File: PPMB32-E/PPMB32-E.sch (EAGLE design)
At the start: 36 parts, among them IC1 7805TV, IC2 LM3940IT-3.3, K1 ARK500/2, K2 ARK500/2, K3 ARK500/2, K4 ARK500/2, K5 ARK500/2, U1 ESP32-DEVKITC-32D

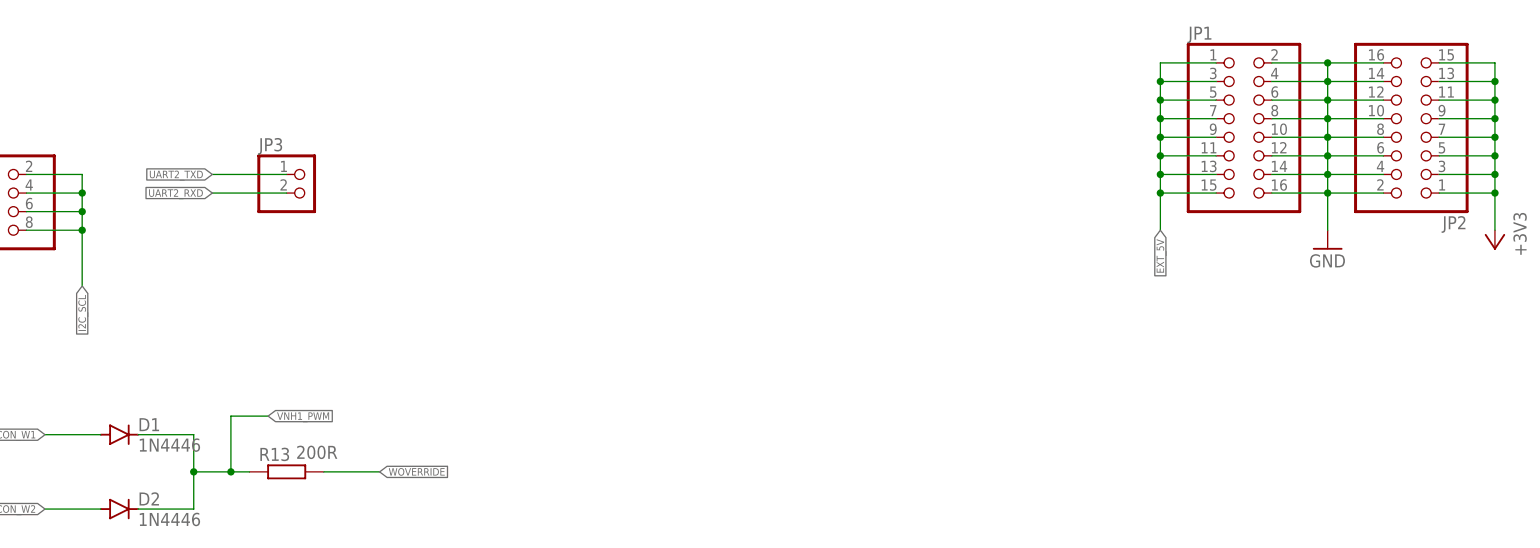
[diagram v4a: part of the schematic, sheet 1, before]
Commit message: Add pins connected to remaining GPIOs on ESP32devkitC
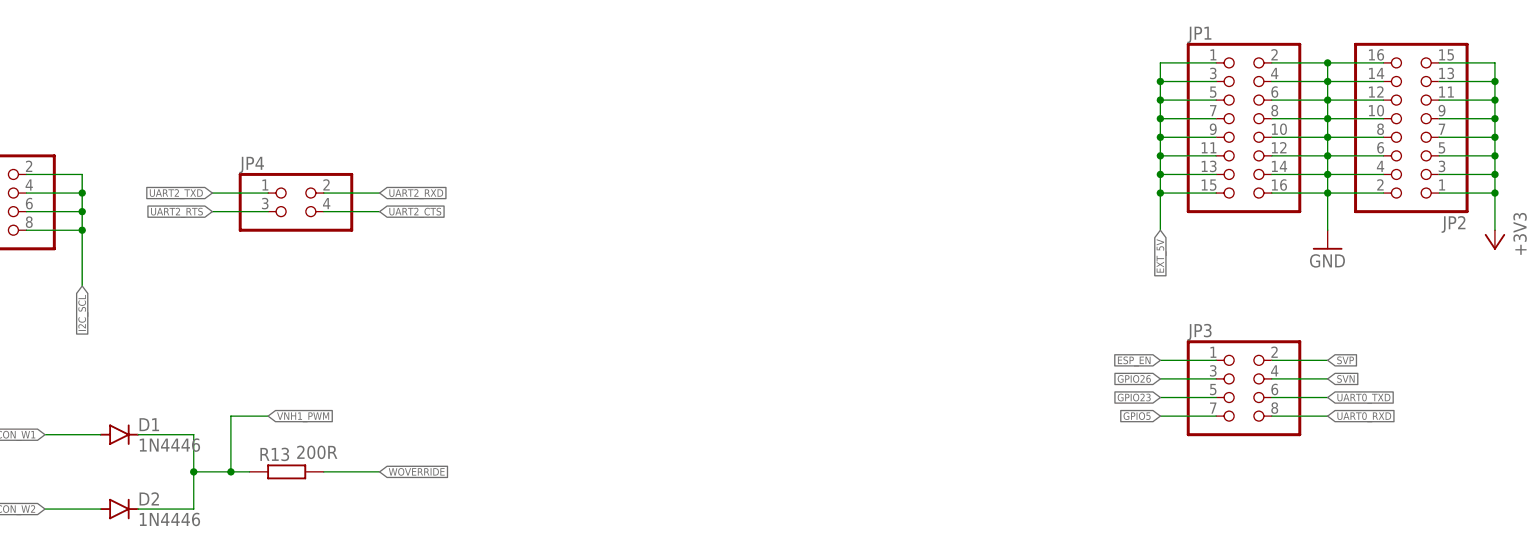
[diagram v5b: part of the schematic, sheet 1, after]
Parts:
- added JP4: (no value), pinhead:PINHD-2X2
- JP3: device pinhead:PINHD-1X2 -> pinhead:PINHD-2X4
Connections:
- net ESP_EN: now also JP3.1
- net GPIO23: now also JP3.5
- net GPIO26: now also JP3.3
- net GPIO5: now also JP3.7
- net SVN: now also JP3.4
- net SVP: now also JP3.2
- net UART0_RXD: now also JP3.8
- net UART0_TXD: now also JP3.6
- net UART2_CTS: now also JP4.4
- net UART2_RTS: now also JP4.3
- net UART2_RXD: now also JP4.2; no longer JP3.2
- net UART2_TXD: now also JP4.1; no longer JP3.1
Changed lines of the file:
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@@
 <setting verticaltext="up"/>
 </settings>
-<grid distance="0.1" unitdist="inch" unit="inch" style="lines" multiple="1" display="no" altdistance="0.01" altunitdist="inch" altunit="inch"/>
+<grid distance="0.1" unitdist="inch" unit="mm" style="lines" multiple="1" display="yes" altdistance="0.01" altunitdist="inch" altunit="mm"/>
 <layers>
 <layer number="1" name="Top" color="4" fill="1" visible="no" active="no"/>
@@
 <part name="R8" library="rcl" library_urn="urn:adsk.eagle:library:334" deviceset="R-EU_" device="R0603" package3d_urn="urn:adsk.eagle:package:23555/3" value="1k"/>
 <part name="GND13" library="supply1" library_urn="urn:adsk.eagle:library:371" deviceset="GND" device=""/>
-<part name="JP3" library="pinhead" library_urn="urn:adsk.eagle:library:325" deviceset="PINHD-1X2" device="" package3d_urn="urn:adsk.eagle:package:22435/2"/>
 <part name="PANCON" library="pinhead" library_urn="urn:adsk.eagle:library:325" deviceset="PINHD-2X6" device="" package3d_urn="urn:adsk.eagle:package:22474/2"/>
 <part name="GND14" library="supply1" library_urn="urn:adsk.eagle:library:371" deviceset="GND" device=""/>
@@
 <part name="GND15" library="supply1" library_urn="urn:adsk.eagle:library:371" deviceset="GND" device=""/>
 <part name="+3V5" library="supply1" library_urn="urn:adsk.eagle:library:371" deviceset="+3V3" device=""/>
+<part name="JP4" library="pinhead" library_urn="urn:adsk.eagle:library:325" deviceset="PINHD-2X2" device="" package3d_urn="urn:adsk.eagle:package:22455/2"/>
+<part name="JP3" library="pinhead" library_urn="urn:adsk.eagle:library:325" deviceset="PINHD-2X4" device="" package3d_urn="urn:adsk.eagle:package:22461/2"/>
 </parts>
 <sheets>
@@
 <attribute name="VALUE" x="312.42" y="160.02" size="1.778" layer="96"/>
 </instance>
-<instance part="JP3" gate="G$1" x="124.46" y="104.14" smashed="yes">
-<attribute name="NAME" x="118.11" y="109.855" size="1.778" layer="95"/>
-<attribute name="VALUE" x="118.11" y="99.06" size="1.778" layer="96"/>
-</instance>
 <instance part="PANCON" gate="A" x="43.18" y="71.12" smashed="yes">
 <attribute name="NAME" x="36.83" y="79.375" size="1.778" layer="95"/>
@@
 <instance part="+3V5" gate="G$1" x="314.96" y="88.9" smashed="yes" rot="R180">
 <attribute name="VALUE" x="312.42" y="88.9" size="1.778" layer="96" rot="R90"/>
+</instance>
+<instance part="JP4" gate="A" x="124.46" y="101.6" smashed="yes">
+<attribute name="NAME" x="115.57" y="107.315" size="1.778" layer="95"/>
+<attribute name="VALUE" x="115.57" y="96.52" size="1.778" layer="96"/>
+</instance>
+<instance part="JP3" gate="A" x="251.46" y="76.2" smashed="yes">
+<attribute name="NAME" x="245.11" y="84.455" size="1.778" layer="95"/>
+<attribute name="VALUE" x="245.11" y="68.58" size="1.778" layer="96"/>
 </instance>
 </instances>
@@
 <label x="83.82" y="195.58" size="1.016" layer="95" rot="R180" xref="yes"/>
 </segment>
+<segment>
+<pinref part="JP3" gate="A" pin="1"/>
+<wire x1="248.92" y1="81.28" x2="241.3" y2="81.28" width="0.1524" layer="91"/>
+<label x="241.3" y="81.28" size="1.016" layer="95" rot="R180" xref="yes"/>
+</segment>
 </net>
 <net name="VNH1_OUTA" class="0">
@@
 <net name="UART2_TXD" class="0">
 <segment>
-<pinref part="JP3" gate="G$1" pin="1"/>
-<wire x1="121.92" y1="106.68" x2="111.76" y2="106.68" width="0.1524" layer="91"/>
-<label x="111.76" y="106.68" size="1.016" layer="95" rot="R180" xref="yes"/>
-</segment>
-<segment>
 <pinref part="U1" gate="G$1" pin="IO16"/>
 <wire x1="132.08" y1="170.18" x2="139.7" y2="170.18" width="0.1524" layer="91"/>
 <label x="139.7" y="170.18" size="1.016" layer="95" xref="yes"/>
 </segment>
+<segment>
+<pinref part="JP4" gate="A" pin="1"/>
+<wire x1="119.38" y1="104.14" x2="111.76" y2="104.14" width="0.1524" layer="91"/>
+<label x="111.76" y="104.14" size="1.016" layer="95" rot="R180" xref="yes"/>
+</segment>
 </net>
 <net name="UART2_RXD" class="0">
-<segment>
-<pinref part="JP3" gate="G$1" pin="2"/>
-<wire x1="121.92" y1="104.14" x2="111.76" y2="104.14" width="0.1524" layer="91"/>
-<label x="111.76" y="104.14" size="1.016" layer="95" rot="R180" xref="yes"/>
-</segment>
 <segment>
 <pinref part="U1" gate="G$1" pin="IO17"/>
 <wire x1="132.08" y1="172.72" x2="139.7" y2="172.72" width="0.1524" layer="91"/>
 <label x="139.7" y="172.72" size="1.016" layer="95" xref="yes"/>
+</segment>
+<segment>
+<pinref part="JP4" gate="A" pin="2"/>
+<wire x1="127" y1="104.14" x2="134.62" y2="104.14" width="0.1524" layer="91"/>
+<label x="134.62" y="104.14" size="1.016" layer="95" xref="yes"/>
 </segment>
 </net>
@@
 <label x="83.82" y="193.04" size="1.016" layer="95" rot="R180" xref="yes"/>
 </segment>
+<segment>
+<pinref part="JP3" gate="A" pin="2"/>
+<wire x1="256.54" y1="81.28" x2="264.16" y2="81.28" width="0.1524" layer="91"/>
+<label x="264.16" y="81.28" size="1.016" layer="95" xref="yes"/>
+</segment>
 </net>
 <net name="SVN" class="0">
@@
 <label x="83.82" y="190.5" size="1.016" layer="95" rot="R180" xref="yes"/>
 </segment>
+<segment>
+<pinref part="JP3" gate="A" pin="4"/>
+<wire x1="256.54" y1="78.74" x2="264.16" y2="78.74" width="0.1524" layer="91"/>
+<label x="264.16" y="78.74" size="1.016" layer="95" xref="yes"/>
+</segment>
 </net>
 <net name="GPIO26" class="0">
@@
 <label x="83.82" y="175.26" size="1.016" layer="95" rot="R180" xref="yes"/>
 </segment>
+<segment>
+<pinref part="JP3" gate="A" pin="3"/>
+<wire x1="248.92" y1="78.74" x2="241.3" y2="78.74" width="0.1524" layer="91"/>
+<label x="241.3" y="78.74" size="1.016" layer="95" rot="R180" xref="yes"/>
+</segment>
 </net>
 <net name="INTERNAL_SENS" class="0">
@@
 <label x="139.7" y="175.26" size="1.016" layer="95" xref="yes"/>
 </segment>
+<segment>
+<pinref part="JP3" gate="A" pin="7"/>
+<wire x1="248.92" y1="73.66" x2="241.3" y2="73.66" width="0.1524" layer="91"/>
+<label x="241.3" y="73.66" size="1.016" layer="95" rot="R180" xref="yes"/>
+</segment>
 </net>
 <net name="UART2_RTS" class="0">
@@
 <label x="139.7" y="177.8" size="1.016" layer="95" xref="yes"/>
 </segment>
+<segment>
+<pinref part="JP4" gate="A" pin="3"/>
+<wire x1="119.38" y1="101.6" x2="111.76" y2="101.6" width="0.1524" layer="91"/>
+<label x="111.76" y="101.6" size="1.016" layer="95" rot="R180" xref="yes"/>
+</segment>
 </net>
 <net name="UART2_CTS" class="0">
@@
 <label x="139.7" y="180.34" size="1.016" layer="95" xref="yes"/>
 </segment>
+<segment>
+<pinref part="JP4" gate="A" pin="4"/>
+<wire x1="127" y1="101.6" x2="134.62" y2="101.6" width="0.1524" layer="91"/>
+<label x="134.62" y="101.6" size="1.016" layer="95" xref="yes"/>
+</segment>
 </net>
 <net name="UART0_RXD" class="0">
@@
 <label x="139.7" y="187.96" size="1.016" layer="95" xref="yes"/>
 </segment>
+<segment>
+<pinref part="JP3" gate="A" pin="8"/>
+<wire x1="256.54" y1="73.66" x2="264.16" y2="73.66" width="0.1524" layer="91"/>
+<label x="264.16" y="73.66" size="1.016" layer="95" xref="yes"/>
+</segment>
 </net>
 <net name="UART0_TXD" class="0">
@@
 <label x="139.7" y="190.5" size="1.016" layer="95" xref="yes"/>
 </segment>
+<segment>
+<pinref part="JP3" gate="A" pin="6"/>
+<wire x1="256.54" y1="76.2" x2="264.16" y2="76.2" width="0.1524" layer="91"/>
+<label x="264.16" y="76.2" size="1.016" layer="95" xref="yes"/>
+</segment>
 </net>
 <net name="GPIO23" class="0">
@@
 <label x="139.7" y="195.58" size="1.016" layer="95" xref="yes"/>
 </segment>
-</net>
+<segment>
+<pinref part="JP3" gate="A" pin="5"/>
+<wire x1="248.92" y1="76.2" x2="241.3" y2="76.2" width="0.1524" layer="91"/>
+<label x="241.3" y="76.2" size="1.016" layer="95" rot="R180" xref="yes"/>
+</segment>
+</net>

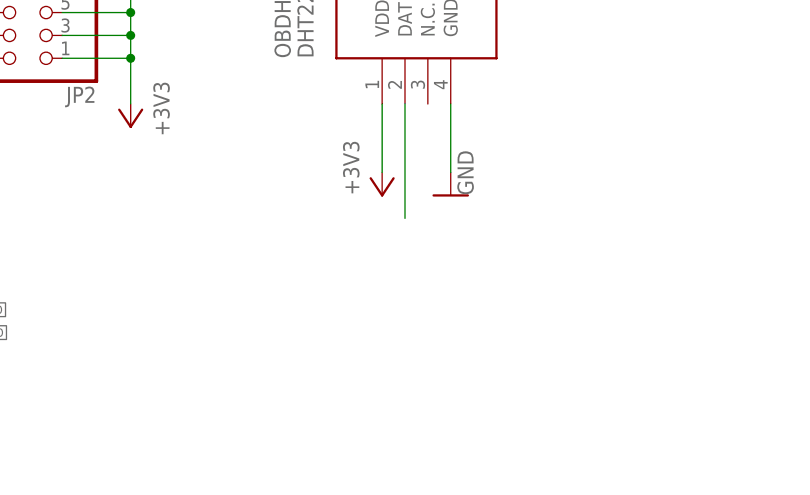
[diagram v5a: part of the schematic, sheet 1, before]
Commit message: Edit silkscreen on PPMB32-E
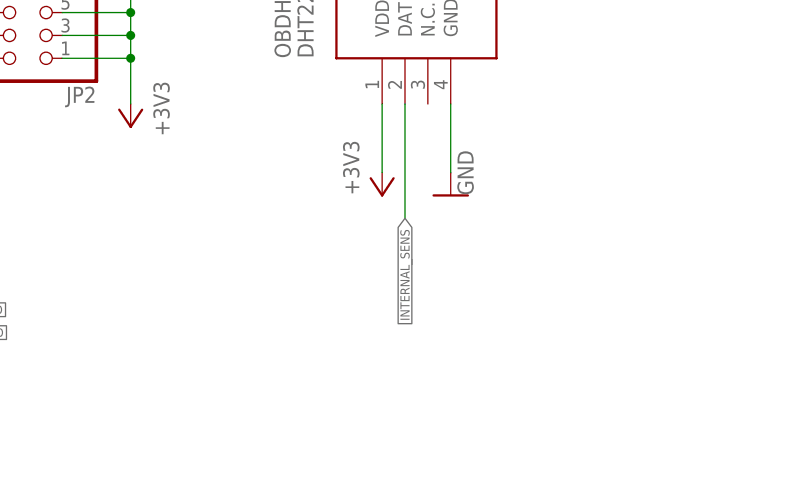
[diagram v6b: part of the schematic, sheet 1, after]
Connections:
- removed net N$13: OBDHT.DAT
- net INTERNAL_SENS: now also OBDHT.DAT
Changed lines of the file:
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@@
 <setting verticaltext="up"/>
 </settings>
-<grid distance="0.1" unitdist="inch" unit="mm" style="lines" multiple="1" display="yes" altdistance="0.01" altunitdist="inch" altunit="mm"/>
+<grid distance="0.1" unitdist="inch" unit="inch" style="lines" multiple="1" display="no" altdistance="0.01" altunitdist="inch" altunit="inch"/>
 <layers>
 <layer number="1" name="Top" color="4" fill="1" visible="no" active="no"/>
@@
 <label x="83.82" y="162.56" size="1.016" layer="95" rot="R180" xref="yes"/>
 </segment>
+<segment>
+<pinref part="OBDHT" gate="G$1" pin="DAT"/>
+<wire x1="317.5" y1="99.06" x2="317.5" y2="86.36" width="0.1524" layer="91"/>
+<label x="317.5" y="86.36" size="1.016" layer="95" rot="R270" xref="yes"/>
+</segment>
 </net>
 <net name="ONE_WIRE" class="0">
@@
 </segment>
 </net>
-<net name="N$13" class="0">
-<segment>
-<pinref part="OBDHT" gate="G$1" pin="DAT"/>
-<wire x1="317.5" y1="99.06" x2="317.5" y2="86.36" width="0.1524" layer="91"/>
-</segment>
-</net>

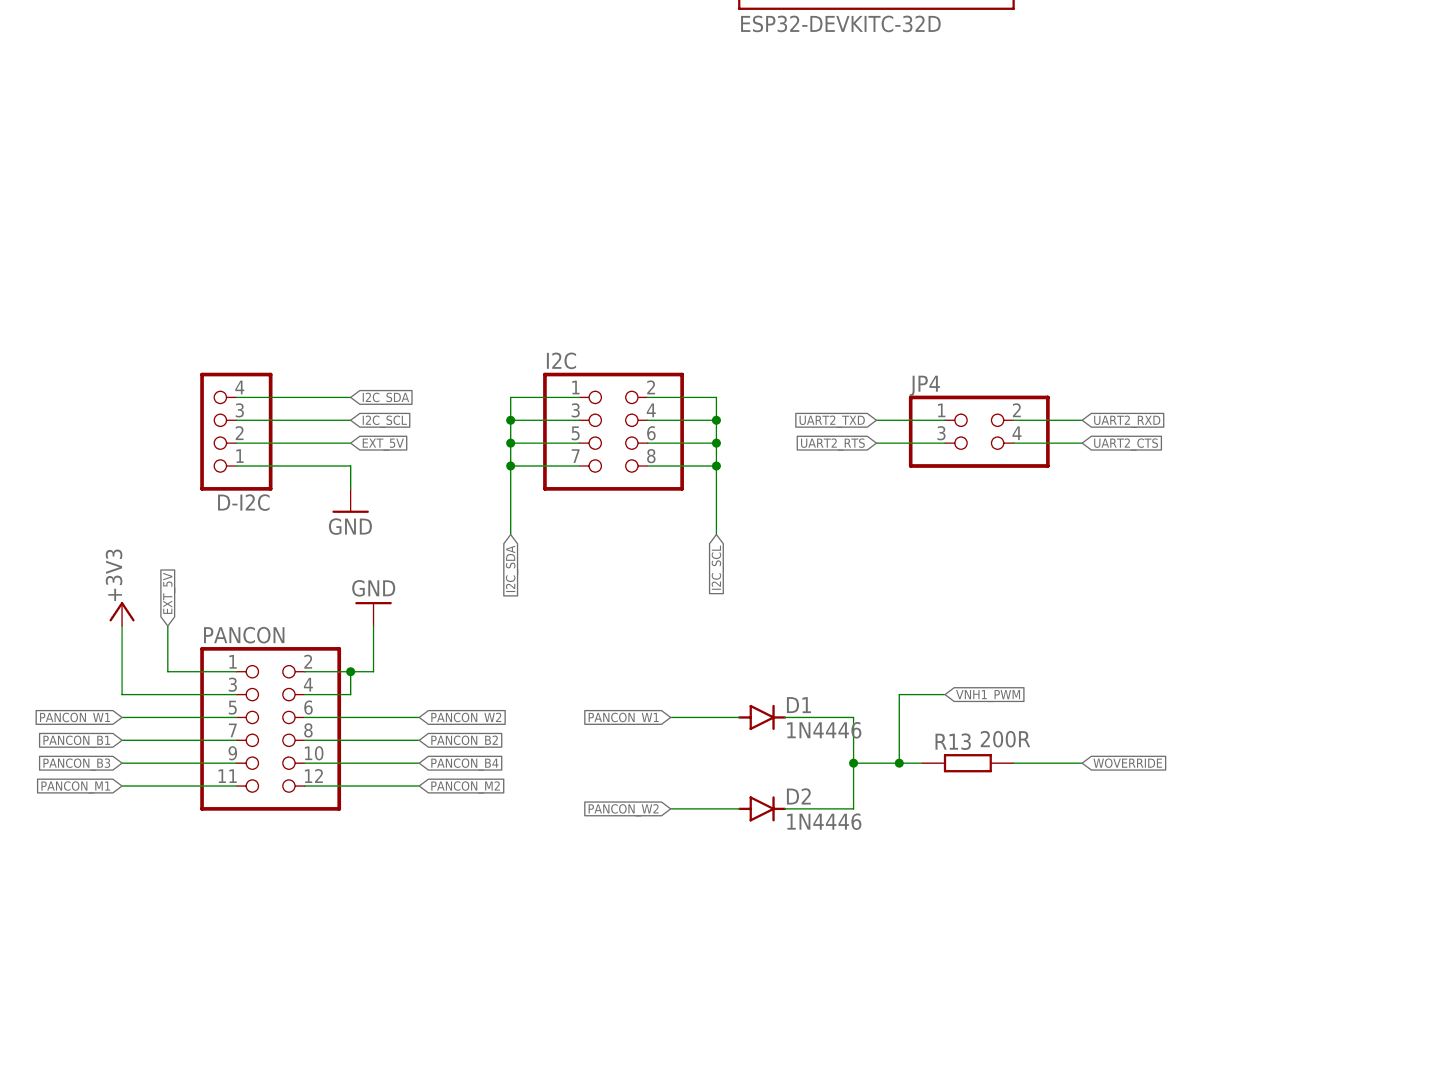
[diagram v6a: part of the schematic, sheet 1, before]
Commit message: Add PanelBoard
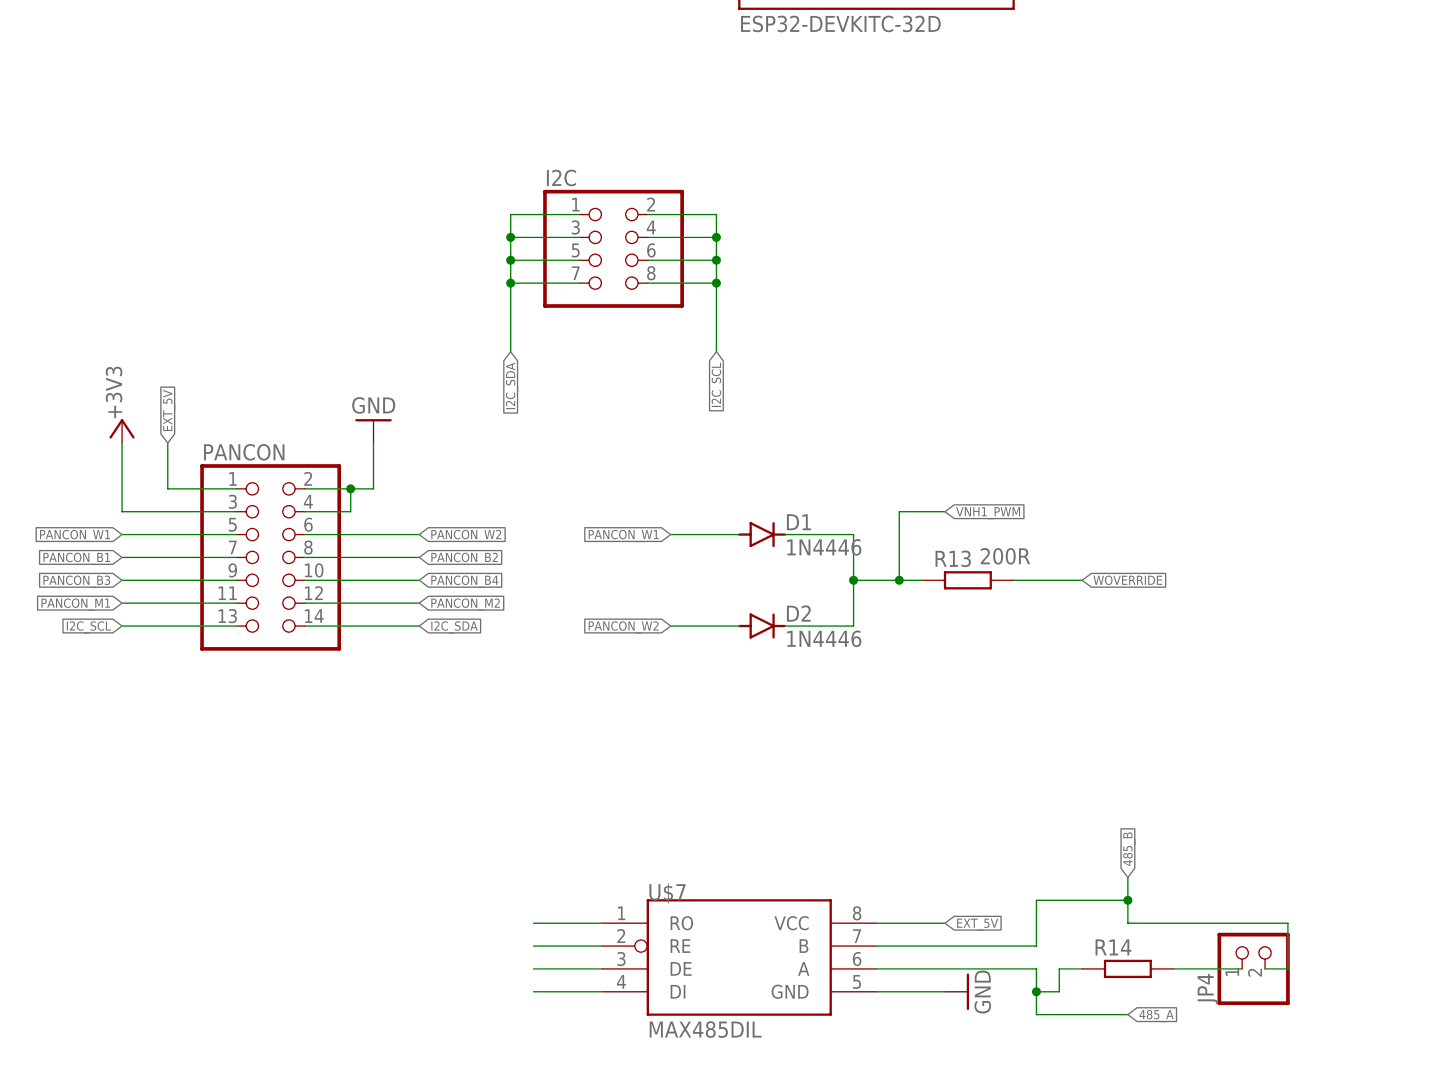
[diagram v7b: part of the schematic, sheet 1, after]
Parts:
- removed D-I2C: (no value), pinhead:PINHD-1X4
- added R14: (no value), rcl:R-EU_R0603
- added U$7: MAX485DIL, MAX485:MAX485DIL
- JP4: device pinhead:PINHD-2X2 -> pinhead:PINHD-1X2/90
- PANCON: device pinhead:PINHD-2X6 -> pinhead:PINHD-2X7
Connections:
- new net 485_A: R14.1, U$7.A
- new net 485_B: JP4.2, U$7.B
- new net N$11: JP4.1, R14.2
- new net N$14: U$7.RO
- new net N$15: U$7.RE
- new net N$16: U$7.DE
- new net N$17: U$7.DI
- net EXT_5V: now also U$7.VCC; no longer D-I2C.2
- net GND: now also U$7.GND; no longer D-I2C.1
- net I2C_SCL: now also PANCON.13; no longer D-I2C.3
- net I2C_SDA: now also PANCON.14; no longer D-I2C.4
- net UART2_CTS: no longer JP4.4
- net UART2_RTS: no longer JP4.3
- net UART2_RXD: no longer JP4.2
- net UART2_TXD: no longer JP4.1
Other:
- moved on the sheet: D1, D2, I2C, R13
